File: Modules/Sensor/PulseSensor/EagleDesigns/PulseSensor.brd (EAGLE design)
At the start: 100 x 80 mm, 11 parts, among them U2 ATMEGA328P_TQFP

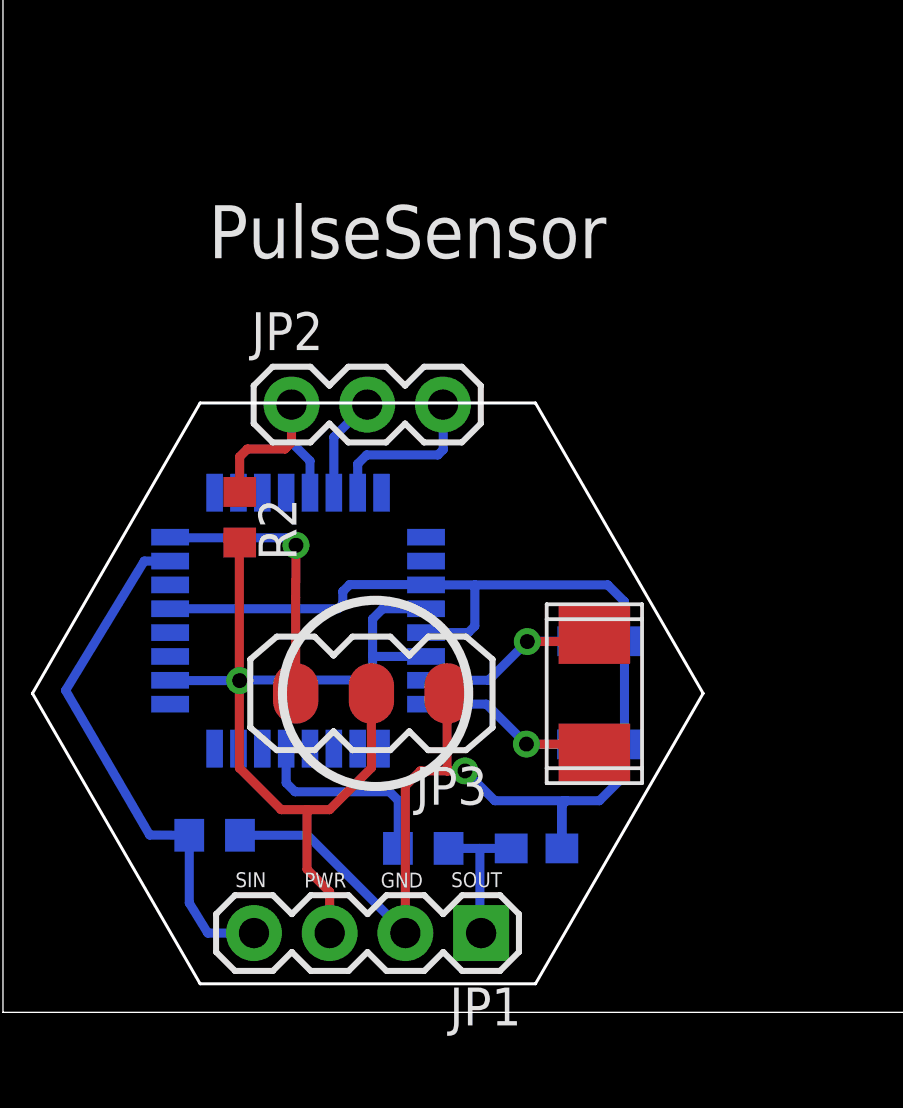
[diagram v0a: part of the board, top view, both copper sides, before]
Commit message: added version numbers, and deleted most of the text that was on each module.
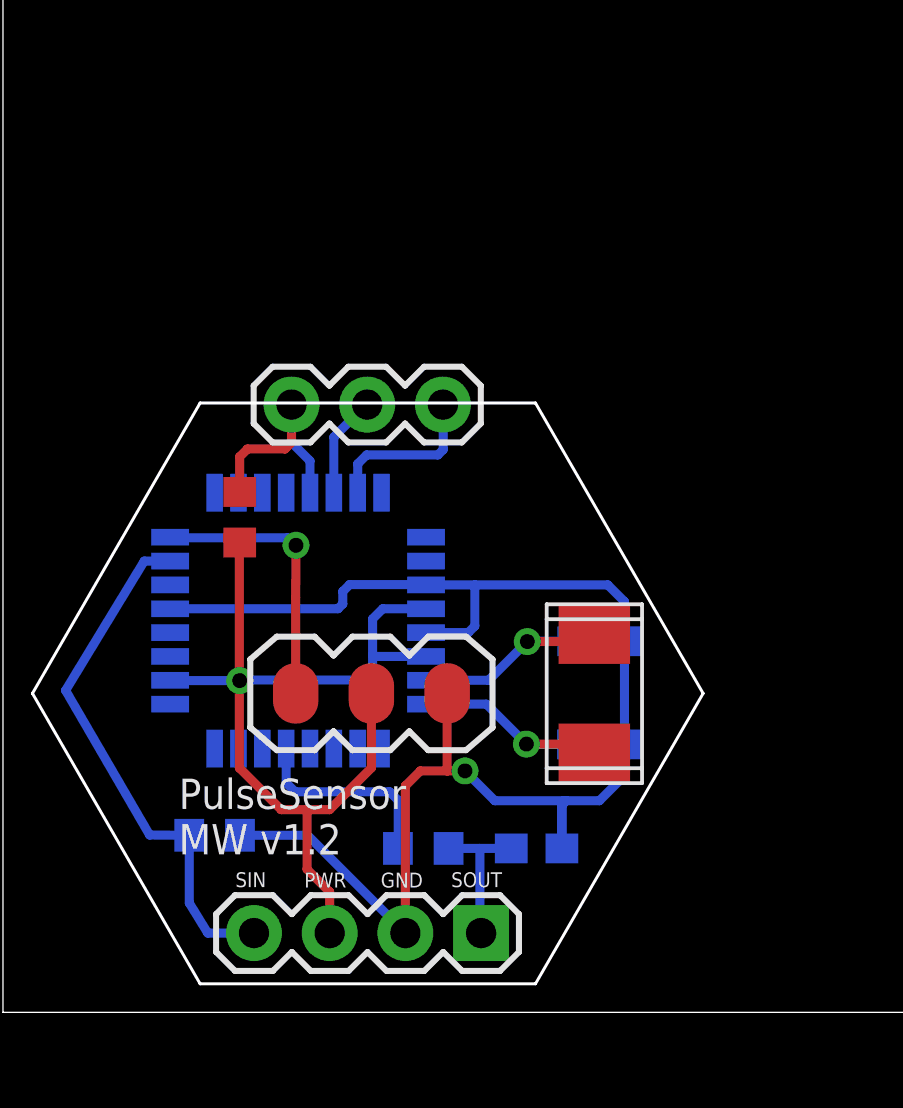
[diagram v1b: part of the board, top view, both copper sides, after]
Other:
- board text added: "PulseSensor MW v1.2"
- board text removed: "PulseSensor"
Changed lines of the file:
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@@
 <layer number="19" name="Unrouted" color="6" fill="1" visible="yes" active="yes"/>
 <layer number="20" name="Dimension" color="15" fill="1" visible="yes" active="yes"/>
-<layer number="21" name="tPlace" color="7" fill="1" visible="no" active="yes"/>
-<layer number="22" name="bPlace" color="7" fill="1" visible="no" active="yes"/>
+<layer number="21" name="tPlace" color="7" fill="1" visible="yes" active="yes"/>
+<layer number="22" name="bPlace" color="7" fill="1" visible="yes" active="yes"/>
 <layer number="23" name="tOrigins" color="15" fill="1" visible="yes" active="yes"/>
 <layer number="24" name="bOrigins" color="15" fill="1" visible="yes" active="yes"/>
-<layer number="25" name="tNames" color="7" fill="1" visible="no" active="yes"/>
-<layer number="26" name="bNames" color="7" fill="1" visible="no" active="yes"/>
-<layer number="27" name="tValues" color="7" fill="1" visible="no" active="yes"/>
-<layer number="28" name="bValues" color="7" fill="1" visible="no" active="yes"/>
+<layer number="25" name="tNames" color="7" fill="1" visible="yes" active="yes"/>
+<layer number="26" name="bNames" color="7" fill="1" visible="yes" active="yes"/>
+<layer number="27" name="tValues" color="7" fill="1" visible="yes" active="yes"/>
+<layer number="28" name="bValues" color="7" fill="1" visible="yes" active="yes"/>
 <layer number="29" name="tStop" color="7" fill="3" visible="no" active="yes"/>
 <layer number="30" name="bStop" color="7" fill="6" visible="no" active="yes"/>
@@
 <text x="12.6723" y="4.188" size="0.5" layer="21">GND</text>
 <text x="15.0345" y="4.2007" size="0.5" layer="21">SOUT</text>
-<text x="6.9" y="25.3" size="1.778" layer="21">PulseSensor</text>
-<circle x="12.5" y="10.7" radius="3.124096875" width="0.3048" layer="21"/>
+<text x="5.9" y="5.3" size="1.016" layer="21">PulseSensor
+MW v1.2</text>
 </plain>
 <attributes>
@@
 </autorouter>
 <elements>
-<element name="C1" library="adafruit" package="C0603" value="22pF" x="20" y="12.45" rot="MR180"/>
-<element name="C2" library="adafruit" package="C0603" value="22pF" x="19.99" y="8.99" rot="MR180"/>
-<element name="JP1" library="SparkFun-Connectors" package="1X04" value="" x="16.04" y="2.66" rot="R180"/>
-<element name="JP2" library="SparkFun-Connectors" package="1X03" value="" x="9.68" y="20.39"/>
-<element name="R1" library="adafruit" package="R0603" value="1M" x="7.1" y="5.94" rot="MR0"/>
-<element name="R2" library="resistor" package="R0603" value="10K" x="7.94" y="16.61" rot="R270"/>
-<element name="U$2" library="MakerWear" package="NX503" value="NX503" x="19.84" y="10.69" rot="R270"/>
-<element name="U2" library="SparkFun-DigitalIC" package="TQFP32-08" value="ATMEGA328P_TQFP" x="9.9" y="13.14" rot="MR0">
+<element name="C1" library="adafruit" package="C0603" value="22pF" x="20" y="12.45" smashed="yes" rot="MR180"/>
+<element name="C2" library="adafruit" package="C0603" value="22pF" x="19.99" y="8.99" smashed="yes" rot="MR180"/>
+<element name="JP1" library="SparkFun-Connectors" package="1X04" value="" x="16.04" y="2.66" smashed="yes" rot="R180">
+<attribute name="VALUE" x="17.31" y="5.835" size="1.27" layer="27" rot="R180"/>
+</element>
+<element name="JP2" library="SparkFun-Connectors" package="1X03" value="" x="9.68" y="20.39" smashed="yes">
+<attribute name="VALUE" x="8.41" y="17.215" size="1.27" layer="27"/>
+</element>
+<element name="R1" library="adafruit" package="R0603" value="1M" x="7.1" y="5.94" smashed="yes" rot="MR0"/>
+<element name="R2" library="resistor" package="R0603" value="10K" x="7.94" y="16.61" smashed="yes" rot="R270"/>
+<element name="U$2" library="MakerWear" package="NX503" value="NX503" x="19.84" y="10.69" smashed="yes" rot="R270"/>
+<element name="U2" library="SparkFun-DigitalIC" package="TQFP32-08" value="ATMEGA328P_TQFP" x="9.9" y="13.14" smashed="yes" rot="MR0">
 <attribute name="PROD_ID" value="IC-09069" x="9.9" y="13.14" size="1.778" layer="28" rot="MR0" display="off"/>
 </element>
-<element name="R4" library="adafruit" package="R0603" value="4.7K" x="14.1" y="5.5" rot="MR0"/>
-<element name="C3" library="adafruit" package="C0603" value="0.22uF" x="17.9" y="5.5" rot="MR180"/>
-<element name="JP3" library="SparkFun-Connectors" package="1X03_NO_HOLES" value="" x="14.9" y="10.7" rot="R180"/>
+<element name="R4" library="adafruit" package="R0603" value="4.7K" x="14.1" y="5.5" smashed="yes" rot="MR0"/>
+<element name="C3" library="adafruit" package="C0603" value="0.22uF" x="17.9" y="5.5" smashed="yes" rot="MR180"/>
+<element name="JP3" library="SparkFun-Connectors" package="1X03_NO_HOLES" value="" x="14.9" y="10.7" smashed="yes" rot="R180">
+<attribute name="VALUE" x="16.17" y="14.51" size="1.27" layer="27" rot="R180"/>
+</element>
 </elements>
 <signals>
@@
 </board>
 </drawing>
+<compatibility>
+<note version="6.3" minversion="6.2.2" severity="warning">
+Since Version 6.2.2 text objects can contain more than one line,
+which will not be processed correctly with this version.
+</note>
+</compatibility>
 </eagle>

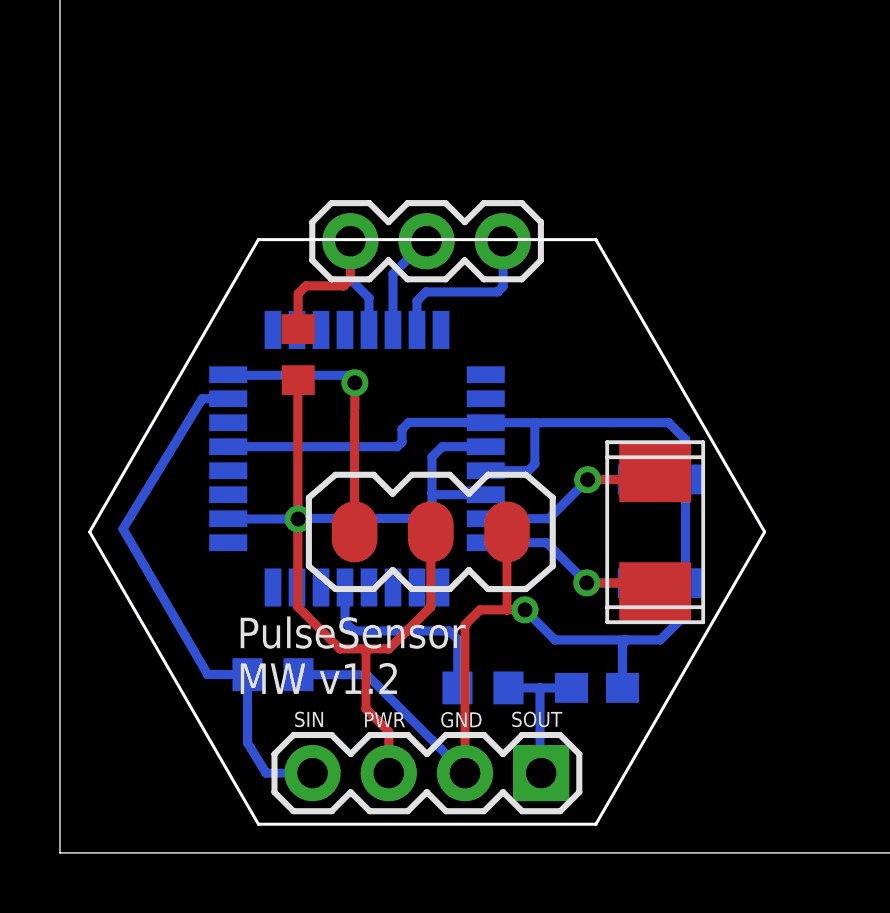
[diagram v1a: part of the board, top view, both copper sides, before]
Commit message: PulseSensor: removed crystal, and modified for new bootloader #40
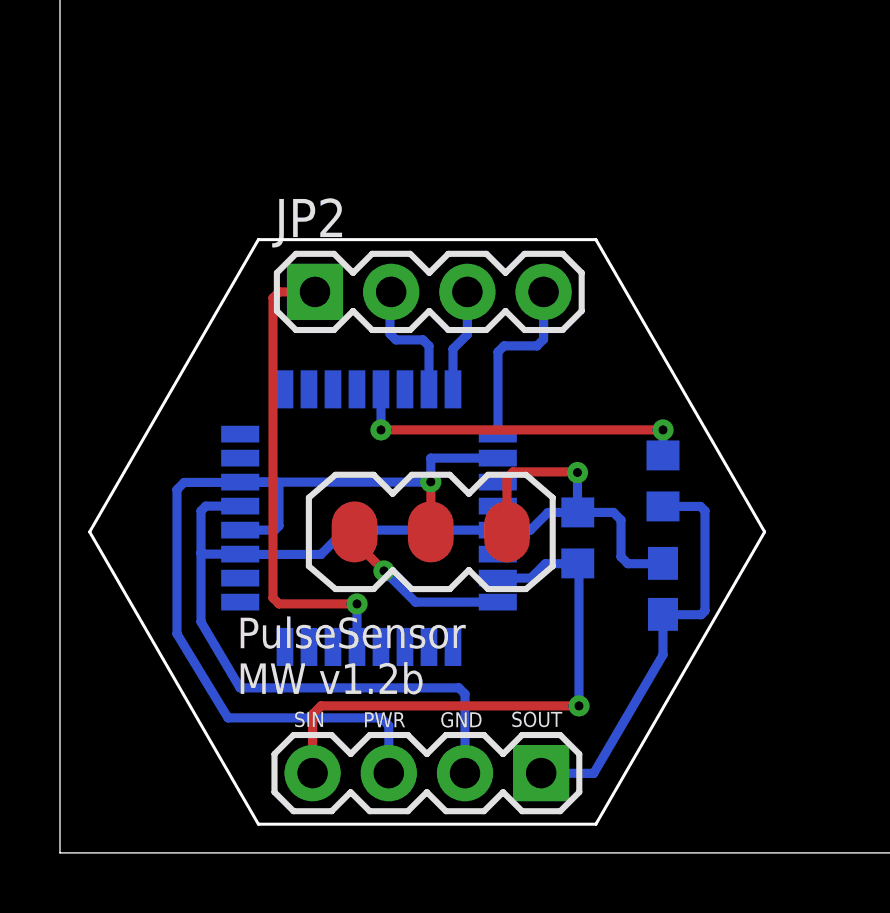
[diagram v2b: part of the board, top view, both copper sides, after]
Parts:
- removed C1, C2: 22pF, adafruit:C0603
- removed R2: 10K, resistor:R0603
- removed U$2: NX503, MakerWear:NX503
- JP2: device SparkFun-Connectors:1X03 -> SparkFun-Connectors:1X04
- moved R1 11.1 mm to (17.3, 10.5), turned to 270 degrees
- moved R4 9.14 mm to (20.1, 12.4), turned to 90 degrees
- moved C3 3.97 mm to (20.1, 8.80), turned to 90 degrees
- moved JP2 2.06 mm to (8.50, 18.7)
- moved U2 2.02 mm to (10.3, 11.2), turned to 180 degrees
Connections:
- removed net N$1: C1.1, U$2.P$1, U2.7
- removed net N$3: C2.1, U$2.P$2, U2.8
- removed net RX: JP2.2, U2.30
- removed net TX: JP2.3, U2.31
- new net MISO: JP2.3, U2.16
- new net MOSI: JP2.2, U2.15
- new net SCK: JP2.4, U2.17
- net GND: no longer C1.2, C2.2
- net RESET: no longer R2.1
- net VCC: no longer R2.2
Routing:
- net GND: track 51.0 -> 40.9 mm
- net 1X3SOUT: track 4.95 -> 13.9 mm
- net RESET: track 7.60 -> 15.8 mm, vias 0 -> 1
- net N$3: track 7.91 -> 0.00 mm, vias 1 -> 0
- net N$1: track 7.85 -> 0.00 mm, vias 1 -> 0
- net SCK: track 0.00 -> 6.02 mm
- net TX: track 5.55 -> 0.00 mm
- net OUT: track 6.76 -> 11.6 mm, vias 0 -> 2
- net MOSI: track 0.00 -> 4.33 mm
- net MISO: track 0.00 -> 3.45 mm
- net RX: track 3.44 -> 0.00 mm
- net PULSE-IN: track 9.35 -> 5.93 mm
- net 1X3SIN: track 17.9 -> 18.6 mm, vias 0 -> 1
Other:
- board text added: "PulseSensor MW v1.2b"
- board text removed: "PulseSensor MW v1.2"
